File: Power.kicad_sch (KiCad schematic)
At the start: 99 parts, among them J2 Molex_Nano-Fit_1x2_SMD_105430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, Q1 SQS401EN-T1_BE3, Q2 SQS401EN-T1_BE3, Q3 SQS401EN-T1_BE3, Q4 PJE138K, Q5 SQS401EN-T1_BE3, Q7 SQS401EN-T1_BE3, Q8 SSM3K15ACT, U1 LTC4412IS6, U2 LTC4412IS6, U3 SIC431AED-T1-GE3, U4 SIC431AED-T1-GE3, U5 SIC431AED-T1-GE3

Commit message: [#81970] Fix 12V power rail, add reset and power-up circuitry
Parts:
- removed C32, C36: C_100n_0402, antmicro-footprints:C_0402_1005Metric, symbol antmicroCapacitors0402:C_100n_0402
- removed Q8: SSM3K15ACT, antmicro-footprints:CST3-3, symbol antmicroTransistorsFETsMOSFETsSingle:SSM3K15ACT
- removed R13: R_20k_0402, antmicro-footprints:R_0402_1005Metric, symbol antmicroResistors0402:R_20k_0402
- removed R14: R_2k7_0402, antmicro-footprints:R_0402_1005Metric, symbol antmicroResistors0402:R_2k7_0402
- removed R18: R_562k_0402, antmicro-footprints:R_0402_1005Metric, symbol antmicroResistors0402:R_562k_0402
- removed R19: R_270k_0402, antmicro-footprints:R_0402_1005Metric, symbol antmicroResistors0402:R_270k_0402
- removed R20: R_39k_0402, antmicro-footprints:R_0402_1005Metric, symbol antmicroResistors0402:R_39k_0402
- added C116, C117, C137: C_10u_0402, antmicro-footprints:C_0402_1005Metric, symbol antmicroCapacitors0402:C_10u_0402
- added C118, C119, C124: C_100n_0402, antmicro-footprints:C_0402_1005Metric, symbol antmicroCapacitors0402:C_100n_0402
- added C134: C_10u_25V_0603, antmicro-footprints:C_0603_1608Metric, symbol antmicroCapacitors0603:C_10u_25V_0603
- added D30: ESD9X5.0ST5G, antmicro-footprints:SOD-923, symbol antmicroTVSDiodes:ESD9X5.0ST5G
- added D36, D37: RB521S30T1G, antmicro-footprints:SOD-523, symbol antmicroDiodesRectifiersSingle:RB521S30T1G
- added D60, D61: TPD1E0B04_XDFN-2, antmicro-footprints:XDFN-2_1x0.60mm, symbol antmicroTVSDiodes:TPD1E0B04_XDFN-2
- added Q10, Q12, Q8 (x2), Q9: PJE138K, antmicro-footprints:SOT-523, symbol antmicroTransistorsFETsMOSFETsSingle:PJE138K
- added Q11: SQS401EN-T1_BE3, antmicro-footprints:Vishay_PowerPAK_1212-8_Single, symbol antmicroTransistorsFETsMOSFETsSingle:SQS401EN-T1_BE3
- added R183, R260: R_0R_0402, antmicro-footprints:R_0402_1005Metric, symbol antmicroResistors0402:R_0R_0402
- added R236: R_200R_0402, antmicro-footprints:R_0402_1005Metric, symbol antmicroResistors0402:R_200R_0402
- added R249: R_100k_0402, antmicro-footprints:R_0402_1005Metric, symbol antmicroResistors0402:R_100k_0402
- added R256: R_1k_0402, antmicro-footprints:R_0402_1005Metric, symbol antmicroResistors0402:R_1k_0402
- added R257, R258, R261: R_200k_0402, antmicro-footprints:R_0402_1005Metric, symbol antmicroResistors0402:R_200k_0402
- added R259, R84: R_10k_0402, antmicro-footprints:R_0402_1005Metric, symbol antmicroResistors0402:R_10k_0402
- added R273: R_0R_0603, antmicro-footprints:R_0603_1608Metric, symbol antmicroResistors0603:R_0R_0603
- added R85: R_0R_22.4A_0603, antmicro-footprints:R_0603_1608Metric, symbol antmicroResistors0603:R_0R_22.4A_0603
- added S4, S5: SW_KMR211NGLFS_SMD, antmicro-footprints:SW_KMR211NGLFS_SMD, symbol antmicroPushbuttonSwitches:SW_KMR211NGLFS_SMD
- added SW1: SW_SPDT_PCM12SMTR, antmicro-footprints:PCM12SMTR, symbol antmicroSlideSwitches:SW_SPDT_PCM12SMTR
- added TP13, TP33, TP52: TP_0.75mm_SMD, antmicro-footprints:TP_SMD_0.75mm, symbol antmicroTestPoints:TP_0.75mm_SMD
- added U37: 74LVC2G14_SOT457, antmicro-footprints:SOT-23-6, symbol antmicroLogicBuffersDriversReceiversTransceivers:74LVC2G14_SOT457
- added U38: 74LVC1G175_SOT457, antmicro-footprints:SOT-23-6, symbol antmicroLogicGatesandInverters:74LVC1G175_SOT457
- added U41: NCP730BMT330_WSON, antmicro-footprints:WSON-6-1EP_2x2mm_P0.65mm, symbol antmicroPMICVoltageRegulatorsLinear:NCP730BMT330_WSON
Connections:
- net +12V: now also Q11.1 (S), Q11.2 (S), Q11.3 (S), R85.2; no longer D7.1 (C), Q7.5 (D), R31.2
- net +3V3: no longer R82.2
- net +5V: now also R82.2, C134.2, U41.4 (EN), U41.6 (V_{IN})
- net 12V_EN: now also Q9.3 (D)
- net 5V_GATE: now also Q10.3 (D), Q11.4 (G), R84.1
- net GND: now also C116.1, C117.1, C118.1, C119.1, C124.1, C134.1, C137.1, D30.2 (A), D60.1 (C), D61.1 (C), Q10.2 (S), Q12.2 (S), Q8.2 (S), Q8.2 (S), Q9.2 (S), R249.1, R261.1, S4.3, S4.4, SW1.S1 (SH), SW1.S2 (SH), SW1.S3 (SH), SW1.S4 (SH), U37.2 (GND), U38.2 (GND), U41.3 (GND), U41.5 (PG), U41.7 (GND)
- net POE: no longer Q7.1 (S), Q7.2 (S), Q7.3 (S), R83.2
- net PoE_STAT: now also Q9.1 (G), TP13.1
- net USBPD0_HV: no longer C25.2, C28.2, C31.1, U5.1 (V_{IN}), U5.2 (V_{IN}), U5.22 (V_{IN}), U5.26 (V_{IN})
- net VCC: now also C25.2, C28.2, C31.1, Q7.1 (S), Q7.2 (S), Q7.3 (S), R83.2, U5.1 (V_{IN}), U5.2 (V_{IN}), U5.22 (V_{IN}), U5.26 (V_{IN})
- net ~{RESET}: now also Q10.1 (G), Q8.3 (D), R183.1, TP33.1
- net at C45.2, C48.2, C51.2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: now also Q7.5 (D)
- new net: D37.2 (A), Q12.3 (D), R259.1, U38.6 (~{CLR})
- new net: C116.2, D36.2 (A), D60.2 (A), Q8.3 (D), R258.1, S4.1, S4.2, SW1.3, U37.1
- new net: R256.1, R257.1, SW1.2
- new net: C117.2, D36.1 (C), R257.2, U37.3
- new net: D7.1 (C), Q11.5 (D), R31.2, R84.2, R85.1
- new net: Q12.1 (G), U37.4
- new net: R258.2, U37.6, U38.1 (CLK)
- new net: D37.1 (C), R236.1
- new net: C124.2, D61.2 (A), Q8.1 (G), R261.2, S5.3, S5.4
- new net: R260.1, U38.4 (Q)
- new net 3V3_LDO: C137.2, R273.1, U41.1 (V_{OUT})
- new net 3V3_STDB: C118.2, C119.2, D30.1 (C), R183.2, R256.2, R259.2, R273.2, S5.1, S5.2, TP52.1, U37.5 (VCC), U38.3 (D), U38.5 (VCC)
- new net POWER_EN: R260.2
- new net PWR_SOFT: Q8.1 (G), R249.2
- new net ~{SHUTDOWN_REQ}: R236.2
- no-connect marks 7 -> 8
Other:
- note added: "3.3V @150mA"
- note added: "Ideal-diode O-Ring"
- note added: "If power source is PoE, which already has an isolated 12V buck converter we want to bypass the SIC431 12V buck converter"
- note added: "MODIFIED CIRCUIT FROM TI's SCEA048B AN"
- note added: "NOTE: SW1 STARTUP CRTL 1-2 AUTO 3-2 MANUAL"
- note added: "POWER BUTTON"
- note added: "POWER-UP AND RESET CIRCUITRY"
- note added: "RESET BUTTON"
- note added: "SHORT PRESS - POWER UP LONG PRESS - POWER DOWN"
- note added: "Soft start"
- note added: "USB controller has an integrated ideal diode"
- note added: "V_{OUT} = 0.6*(191k+10k)/10k = 12.06[V]"
- moved on the sheet: C33, C34, C35, C37, C38, C39, C40, C41, C42, C43, C44, C45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

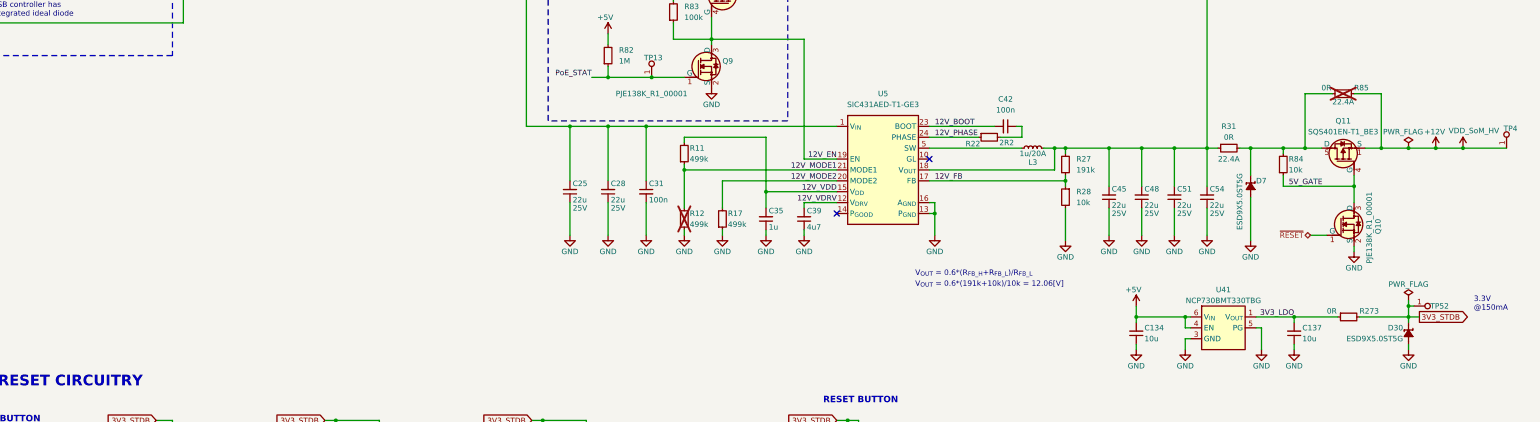
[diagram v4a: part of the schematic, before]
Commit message: [#81970] Add power sequencing IC
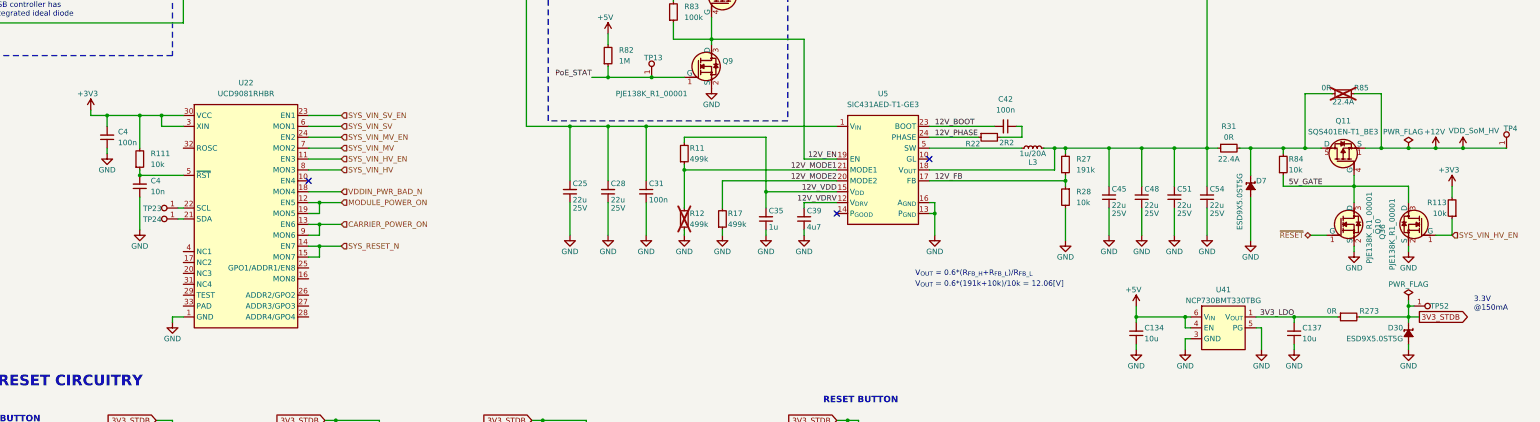
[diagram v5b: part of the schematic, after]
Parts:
- added C4: C_10n_0603, antmicro-footprints:C_0603_1608Metric, symbol antmicroCapacitors0603:C_10n_0603
- added C4: C_100n_16V_X7R_0402, antmicro-footprints:C_0402_1005Metric, symbol antmicroCapacitors0402:C_100n_16V_X7R_0402
- added Q36: PJE138K, antmicro-footprints:SOT-523, symbol antmicroTransistorsFETsMOSFETsSingle:PJE138K
- added R111, R113: R_10k_0402, antmicro-footprints:R_0402_1005Metric, symbol antmicroResistors0402:R_10k_0402
- added TP23, TP24: TP_0.75mm_SMD, antmicro-footprints:TP_SMD_0.75mm, symbol antmicroTestPoints:TP_0.75mm_SMD
- added U22: UCD9081, antmicro-footprints:HVQFN-32-1EP_5x5mm_P0.5mm_EP3.6x3.6mm, symbol antmicroPMICPowerSequencers:UCD9081
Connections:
- net +3V3: now also C4.2, R111.2, R113.2, U22.3 (XIN), U22.30 (VCC)
- net 5V_GATE: now also Q36.3 (D)
- net GND: now also C4.1, C4.1, Q36.2 (S), U22.1 (GND)
- new net: TP23.1, U22.22 (SCL)
- new net: TP24.1, U22.21 (SDA)
- new net: C4.2, R111.1, U22.5 (~{RST})
- new net CARRIER_POWER_ON: U22.13 (EN6), U22.9 (MON6)
- new net MODULE_POWER_ON: U22.12 (EN5), U22.19 (MON5)
- new net SYS_RESET_N: U22.14 (EN7), U22.15 (MON7)
- new net SYS_VIN_HV: U22.8 (MON3)
- new net SYS_VIN_HV_EN: Q36.1 (G), R113.1, U22.11 (EN3)
- new net SYS_VIN_MV: U22.7 (MON2)
- new net SYS_VIN_MV_EN: U22.24 (EN2)
- new net SYS_VIN_SV: U22.6 (MON1)
- new net SYS_VIN_SV_EN: U22.23 (EN1)
- new net VDDIN_PWR_BAD_N: U22.18 (MON4)
- no-connect marks 8 -> 9

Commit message: [#81970] Drop PoE
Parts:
- removed C18: C_100n_50V_X8L_0402, antmicro-footprints:C_0402_1005Metric, symbol antmicroCapacitors0402:C_100n_50V_X8L_0402
- removed C20: C_1u_25V_0402, antmicro-footprints:C_0402_1005Metric, symbol antmicroCapacitors0402:C_1u_25V_0402
- removed D2: DF2S30FS_SOD, antmicro-footprints:SOD-923, symbol antmicroTVSDiodes:DF2S30FS_SOD
- removed Q2, Q7: SQS401EN-T1_BE3, antmicro-footprints:Vishay_PowerPAK_1212-8_Single, symbol antmicroTransistorsFETsMOSFETsSingle:SQS401EN-T1_BE3
- removed Q9: PJE138K, antmicro-footprints:SOT-523, symbol antmicroTransistorsFETsMOSFETsSingle:PJE138K
- removed R82: R_1M_0402, antmicro-footprints:R_0402_1005Metric, symbol antmicroResistors0402:R_1M_0402
- removed R83: R_100k_0201, antmicro-footprints:R_0201, symbol antmicroResistorsmisc:R_100k_0201
- removed TP13: TP_0.75mm_SMD, antmicro-footprints:TP_SMD_0.75mm, symbol antmicroTestPoints:TP_0.75mm_SMD
- removed U2: LTC4412IS6, antmicro-footprints:SOT-23-6, symbol antmicroPMICORControllersIdealDiodes:LTC4412IS6
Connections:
- net 12V_EN is gone; now on net VCC: U5.19 (EN)
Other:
- note removed: "If power source is PoE, which already has an isolated 12V buck converter we want to bypass the SIC431 12V buck converter"
- moved on the sheet: C134, C137, C25, C28, C31, C35, C39, C4, C42, C45, C48, C51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

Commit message: [#81970] Add reverse polarity protection, Power sequencing
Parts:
- removed D1: DF2S30FS_SOD, antmicro-footprints:SOD-923, symbol antmicroTVSDiodes:DF2S30FS_SOD
- removed Q10, Q4: PJE138K, antmicro-footprints:SOT-523, symbol antmicroTransistorsFETsMOSFETsSingle:PJE138K
- removed R183, R21: R_0R_0402, antmicro-footprints:R_0402_1005Metric, symbol antmicroResistors0402:R_0R_0402
- removed R32: R_10k_0402, antmicro-footprints:R_0402_1005Metric, symbol antmicroResistors0402:R_10k_0402
- removed R33, R85: R_0R_22.4A_0603, antmicro-footprints:R_0603_1608Metric, symbol antmicroResistors0603:R_0R_22.4A_0603
- removed TP23, TP24, TP5: TP_0.75mm_SMD, antmicro-footprints:TP_SMD_0.75mm, symbol antmicroTestPoints:TP_0.75mm_SMD
- added BT1: Battery_Holder_MS621FE-FL11E, antmicro-footprints:MS621FE-FL11E, symbol antmicroBatteryHoldersClipsContacts:Battery_Holder_MS621FE-FL11E
- added D13: BZX84C5V1-TP, antmicro-footprints:SOT-23-3, symbol antmicroDiodesZenerSingle:BZX84C5V1-TP
- added D14: DF2S30FS_SOD, antmicro-footprints:SOD-923, symbol antmicroTVSDiodes:DF2S30FS_SOD
- added D34: RB521S30T1G, antmicro-footprints:SOD-523, symbol antmicroDiodesRectifiersSingle:RB521S30T1G
- added Q12, Q16: SQS401EN-T1_BE3, antmicro-footprints:Vishay_PowerPAK_1212-8_Single, symbol antmicroTransistorsFETsMOSFETsSingle:SQS401EN-T1_BE3
- added Q13, Q14: PJE138K, antmicro-footprints:SOT-523, symbol antmicroTransistorsFETsMOSFETsSingle:PJE138K
- added Q20: SSM3J332R, antmicro-footprints:SOT-23-3, symbol antmicroTransistorsFETsMOSFETsSingle:SSM3J332R
- added R294: R_2k2_0402, antmicro-footprints:R_0402_1005Metric, symbol antmicroResistors0402:R_2k2_0402
- added R44, R46, R47, R49, R53, R55, R57, R59, R60, R69: R_10k_0402, antmicro-footprints:R_0402_1005Metric, symbol antmicroResistors0402:R_10k_0402
- added R45, R62, R64, R66: R_100k_0402, antmicro-footprints:R_0402_1005Metric, symbol antmicroResistors0402:R_100k_0402
- added R51: R_22k_0402, antmicro-footprints:R_0402_1005Metric, symbol antmicroResistors0402:R_22k_0402
- added R72: R_1k_0402, antmicro-footprints:R_0402_1005Metric, symbol antmicroResistors0402:R_1k_0402
- added TP2: TP_0.75mm_SMD, antmicro-footprints:TP_SMD_0.75mm, symbol antmicroTestPoints:TP_0.75mm_SMD
- R?: renamed from R12; now fitted
- R?: renamed from R11; now not fitted
- renumbered C4 to C85, C134 to C?, C51 to C?, C22 to C?, C31 to C?, C43 to C?, C118 to C?, C23 to C?, C46 to C?, C54 to C?, C38 to C?, C137 to C?, C29 to C?, C40 to C?, C48 to C?, C30 to C?, C124 to C?, C117 to C?, C37 to C?, C27 to C?, C44 to C?, C17 to C?, C34 to C?, C33 to C?, C119 to C?, C25 to C?, C28 to C?, C53 to C?, C26 to C?, C50 to C?, C52 to C?, C19 to C?, C49 to C?, C45 to C?, C35 to C?, C39 to C?, C42 to C?, C47 to C?, C41 to C?, C21 to C?, C24 to C?, C116 to C?, D5 to D?, D3 to D?, D37 to D?, D6 to D?, D61 to D?, D7 to D?, D36 to D?, D30 to D?, D4 to D?, D60 to D?, J2 to J?, L3 to L?, L2 to L?, L1 to L?, Q36 to Q37, Q5 to Q?, Q1 to Q?, Q12 to Q?, Q8 to Q?, Q3 to Q?, Q11 to Q?, R111 to R112, R113 to R114, R259 to R?, R8 to R?, R15 to R?, R6 to R?, R7 to R?, R257 to R?, R25 to R?, R256 to R?, R27 to R?, R9 to R?, R31 to R?, R17 to R?, R28 to R?, R260 to R?, R23 to R?, R29 to R?, R26 to R?, R258 to R?, R10 to R?, R3 to R?, R5 to R?, R4 to R?, R24 to R?, R261 to R?, R16 to R?, R236 to R?, R249 to R?, R273 to R?, R84 to R?, R30 to R?, R22 to R?, S4 to S?, S5 to S?, SW1 to SW?, TP4 to TP?, TP52 to TP?, TP2 to TP?, TP33 to TP?, TP1 to TP?, TP3 to TP?, U22 to U23, U1 to U?, U41 to U?, U37 to U?, U38 to U?, U5 to U?, U3 to U?, U4 to U?
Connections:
- net 5V_EN is gone; now on net ~{PERIPHERAL_RESET}: U?.19 (EN)
- net SYS_VIN_SV is gone; now on net +3V3: U23.6 (MON1)
- net ~{RESET} is gone; now on net ~{PERIPHERAL_RESET}: Q?.3 (D), TP?.1
- net +12V: now also R51.2
- net +3V3: now also Q12.1 (S), Q12.2 (S), Q12.3 (S), R62.2; no longer D?.1 (C), R114.2, R?.2, TP?.1
- net +5V: now also R55.2, TP2.1
- net 3V3_STDB: now also D34.2 (A), R69.2
- net 5V_GATE: now also Q12.4 (G), Q13.3 (D), Q14.3 (D), R44.1, R59.1
- net CARRIER_POWER_ON: no longer U23.13 (EN6)
- net DC_IN: now also D13.3 (C), Q16.1 (S), Q16.2 (S), Q16.3 (S); no longer J?.1
- net GND: now also R114.1, U23.29 (TEST), U23.33 (PAD), BT1.2 (-), D14.2 (A), Q13.2 (S), Q14.2 (S), Q20.3 (D), R46.1, R47.1, R49.1, R53.1, R57.1, R60.1, R72.1
- net MODULE_POWER_ON: now also R49.2
- net POWER_EN: now also Q20.1 (G)
- net SYS_VIN_HV_EN: now also R114.2; no longer R114.1
- net SYS_VIN_MV_EN: now also Q13.1 (G), R46.2
- net SYS_VIN_SV_EN: now also Q14.1 (G), R60.2
- net VCC: now also R45.2, R64.2, R66.2; no longer U?.19 (EN)
- net VDDIN_PWR_BAD_N: now also R47.2
- net SYS_I2C_CLK: now reaches U23.22 (SCL)
- net SYS_I2C_DAT: now reaches U23.21 (SDA)
- net at U23.32 (ROSC): now also R62.1
- net +5V_SoM: no longer names the net of D?.1 (C), Q?.5 (D), R?.2
- net +5V_SoM: now also R44.2
- net 3V3_EN renamed ~{PERIPHERAL_RESET}
- net ~{PERIPHERAL_RESET}: now also U?.19 (EN), Q20.2 (S), R45.1, R64.1, R66.1, R69.1
- net SYS_RESET_N: no longer names the net of U23.14 (EN7)
- net SYS_RESET_N: no longer U23.15 (MON7)
- net SYS_VIN_HV: no longer names the net of U23.8 (MON3)
- net SYS_VIN_HV: now also R51.1, R53.2
- net SYS_VIN_MV: no longer names the net of U23.7 (MON2)
- net SYS_VIN_MV: now also R55.1, R57.2
- net ~{SHUTDOWN_REQ} renamed ~{MODULE_SHDN_N}
- new net: D13.1 (A), Q16.4 (G), R72.2
- new net: BT1.1 (+), R294.1
- new net: D14.1 (C), J?.1, Q16.5 (D)
- new net +3V3_AON: D?.1 (C), Q12.5 (D), R59.2, R?.2, TP?.1
- new net PMIC_BBATT: D34.1 (C), R294.2
- no-connect marks 9 -> 21
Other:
- note added: "Power sequencer"
- note added: "R70 > 5.1 * (20-5.1)/0.350 > 217 Ohm"
- moved on the sheet: C4, C85, C?, D?, J?, L?, Q37, Q?, R112, R114, R?, S?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

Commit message: [#82055] Add USB recovery port
[#81970] add discharge circuit

[#81970] Annotation

[#81782] Annotation and clean up
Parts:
- removed D13: BZX84C5V1-TP, antmicro-footprints:SOT-23-3, symbol antmicroDiodesZenerSingle:BZX84C5V1-TP
- removed Q16: SQS401EN-T1_BE3, antmicro-footprints:Vishay_PowerPAK_1212-8_Single, symbol antmicroTransistorsFETsMOSFETsSingle:SQS401EN-T1_BE3
- removed R72: R_1k_0402, antmicro-footprints:R_0402_1005Metric, symbol antmicroResistors0402:R_1k_0402
- added Q7, Q8: PJE138K, antmicro-footprints:SOT-523, symbol antmicroTransistorsFETsMOSFETsSingle:PJE138K
- added R10, R37, R39: R_10k_0402, antmicro-footprints:R_0402_1005Metric, symbol antmicroResistors0402:R_10k_0402
- added R40, R45, R48: R_470R_0402, antmicro-footprints:R_0402_1005Metric, symbol antmicroResistors0402:R_470R_0402
- gave numbers to parts that had none: 111
- renumbered C85 to C1, C4 to C2, D14 to D1, D34 to D11, Q37 to Q11, Q13 to Q12, Q12 to Q13, Q20 to Q5, R112 to R1, R55 to R14, R57 to R15, R51 to R17, R53 to R18, R62 to R2, R69 to R33, R64 to R34, R66 to R35, R45 to R36, R44 to R53, R294 to R54, R59 to R55, R114 to R57, R46 to R58, R60 to R59, R47 to R6, R49 to R8, TP2 to TP6, U23 to U1
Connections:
- net +12V: now also R45.2
- net +3V3: now also R48.2; no longer C1.2, R1.2, R2.2, U1.3 (XIN), U1.30 (VCC)
- net +3V3_AON: now also C1.2, R1.2, R2.2, U1.3 (XIN), U1.30 (VCC)
- net +5V: now also R40.2; no longer C52.2, U8.4 (EN), U8.6 (V_{IN})
- net 3V3_STDB: now also R39.2
- net CARRIER_POWER_ON: now also R10.2
- net DC_IN: now also D1.1 (C), J2.1
- net GND: now also Q7.2 (S), Q8.2 (S), R10.1, R37.1
- net MODULE_POWER_ON: now also Q7.1 (G), R37.2
- net VCC: now also C52.2, U8.4 (EN), U8.6 (V_{IN})
- net 12V_OUT: now reaches C48.2, C51.2, C55.2, C58.2, L3.2, R46.2, R50.1, U7.18 (V_{OUT})
- net ~{PERIPHERAL_RESET} renamed 12V_EN
- new net: Q7.3 (D), Q8.1 (G), R39.1
- new net: Q8.3 (D), R40.1, R45.1, R48.1
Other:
- note added: "12V @12A"
- note added: "DISCHARGE CIRCUIT"
- note added: "RTC BACK-UP POWER"
- note removed: "R70 > 5.1 * (20-5.1)/0.350 > 217 Ohm"
- moved on the sheet: BT1, C1, C2, C36, D11, D7, Q6, R1, R14, R15, R17, R18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
